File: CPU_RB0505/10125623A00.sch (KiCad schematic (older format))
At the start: 0 parts

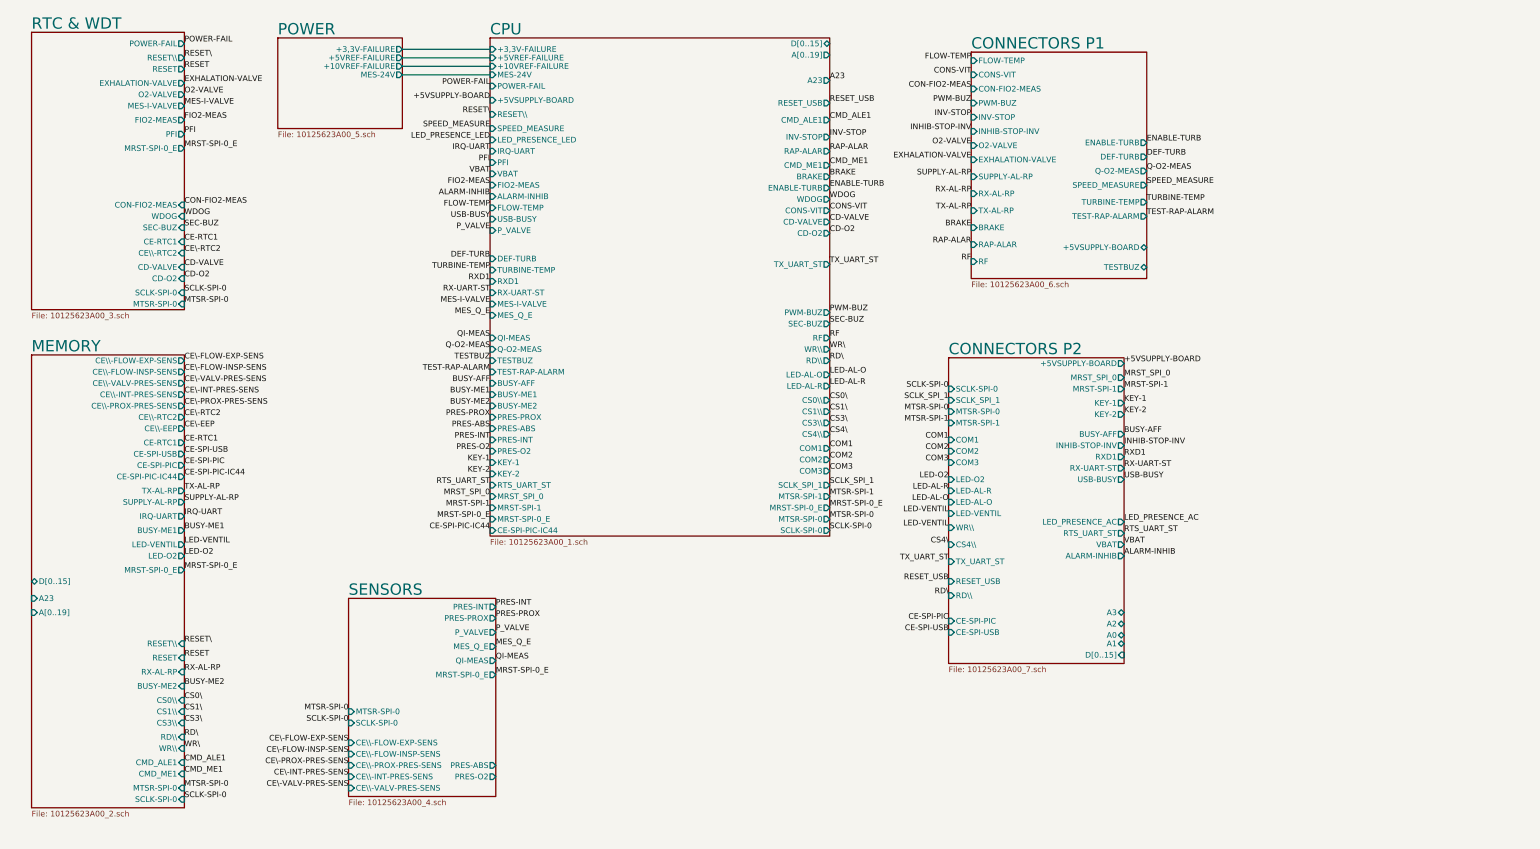
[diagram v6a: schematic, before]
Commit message: Connected busses
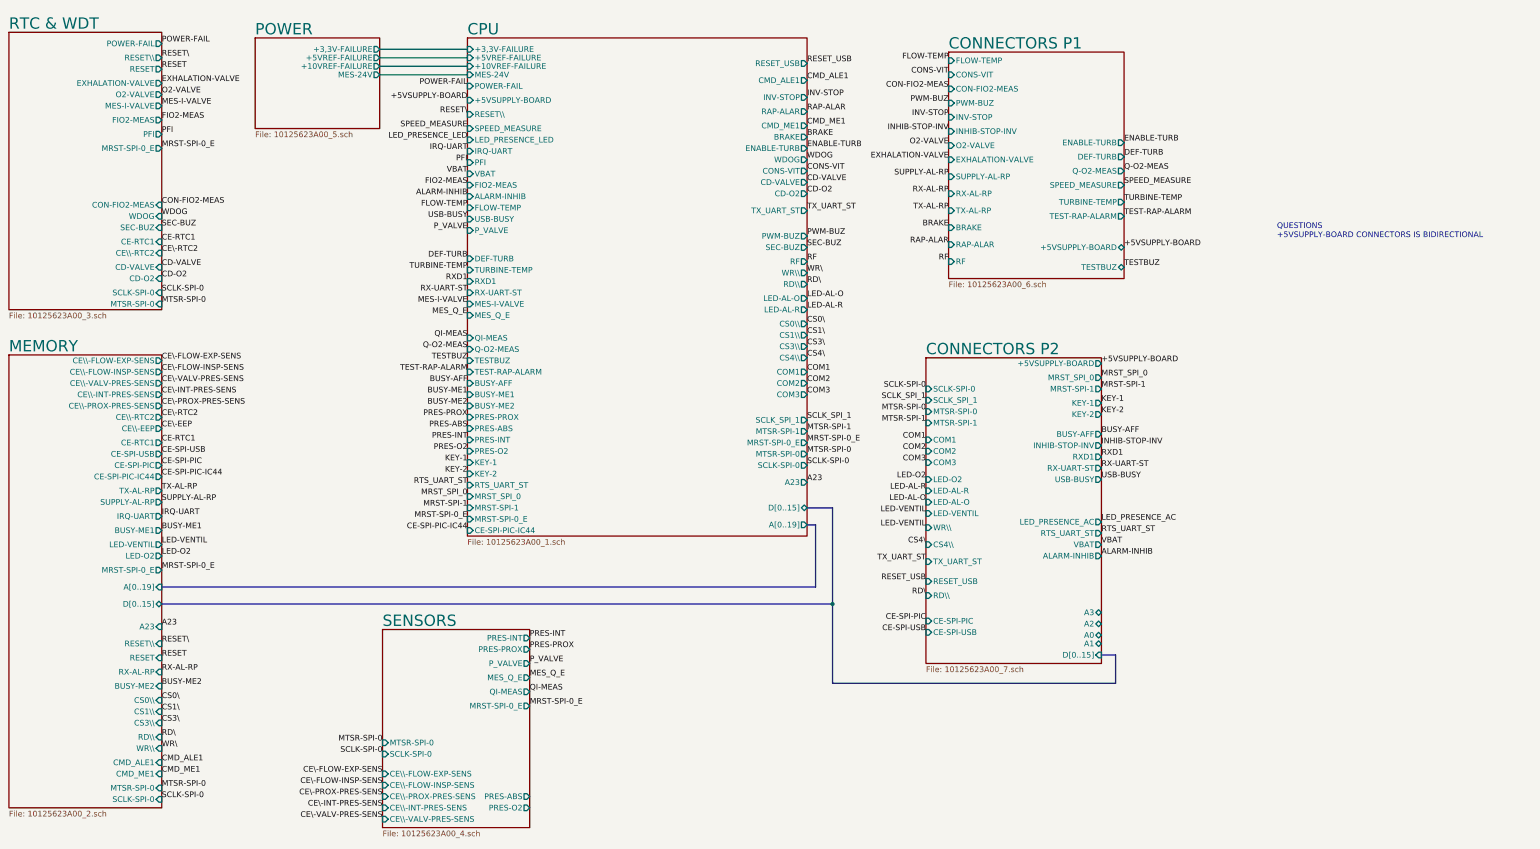
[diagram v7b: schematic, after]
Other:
- note added: "QUESTIONS\n+5VSUPPLY-BOARD CONNECTORS IS BIDIRECTIONAL"

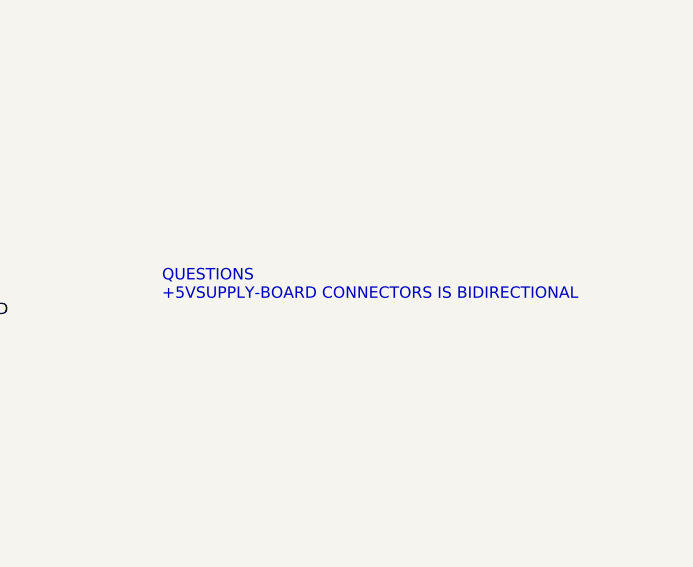
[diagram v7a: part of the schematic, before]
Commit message: Deleted WIP comments and reviewed remaining ERC errors
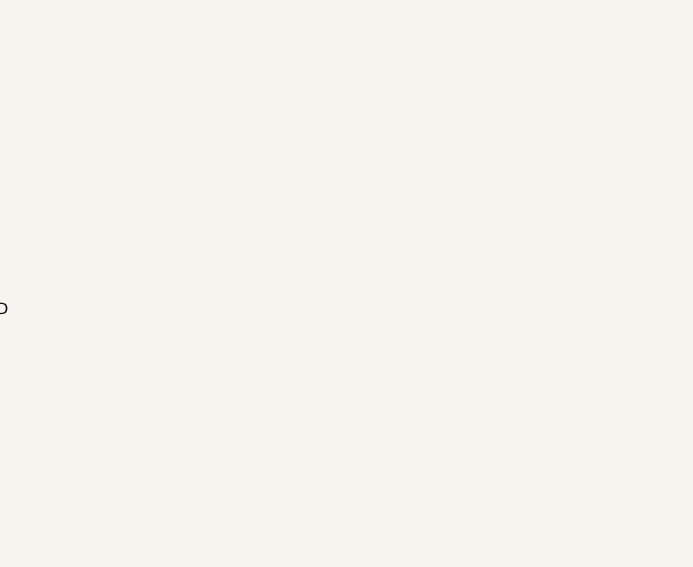
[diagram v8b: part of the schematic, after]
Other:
- note removed: "QUESTIONS\n+5VSUPPLY-BOARD CONNECTORS IS BIDIRECTIONAL"
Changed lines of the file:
@@
 Text Label 10450 2550 0    50   ~ 0
 +5VSUPPLY-BOARD
-Text Notes 11800 2475 0    50   ~ 0
-QUESTIONS\n+5VSUPPLY-BOARD CONNECTORS IS BIDIRECTIONAL
 Text Label 10450 2725 0    50   ~ 0
 TESTBUZ
